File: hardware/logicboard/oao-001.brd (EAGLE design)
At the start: 100 x 80 mm, 9 parts, among them K1 G5V1, T1 2SC1815

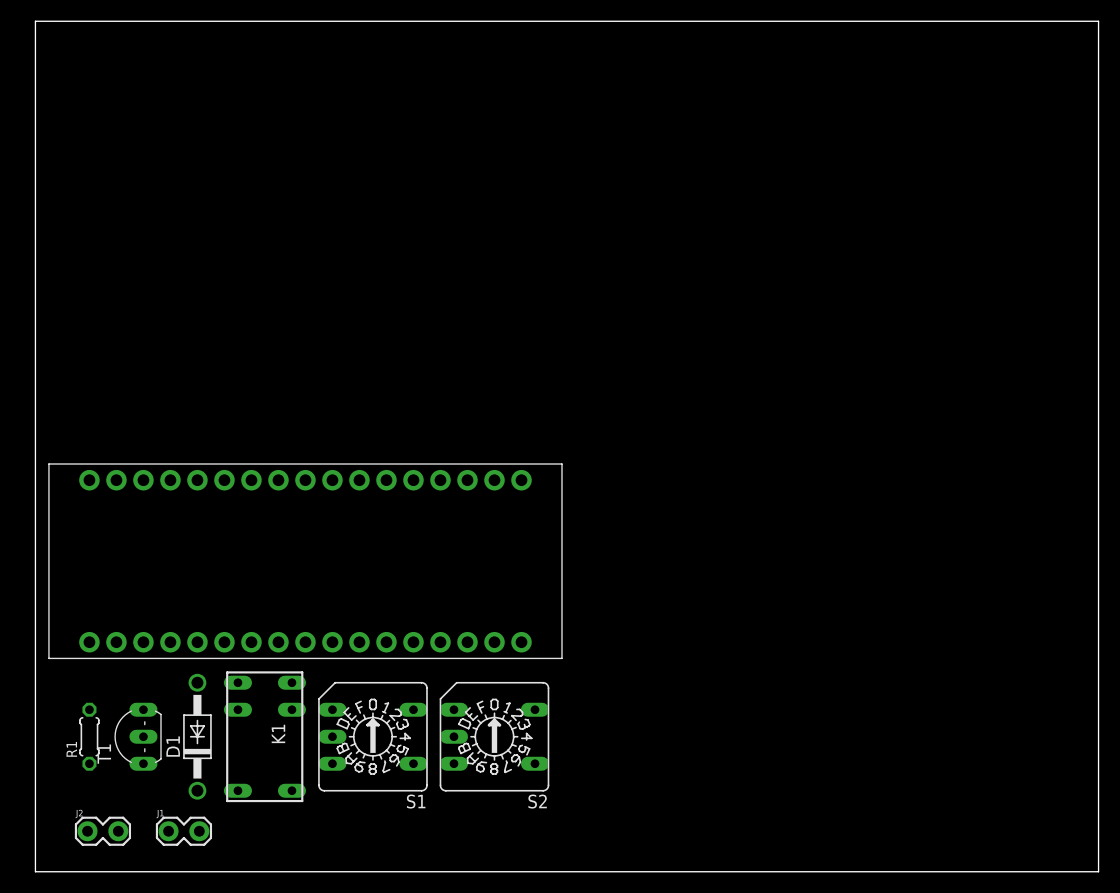
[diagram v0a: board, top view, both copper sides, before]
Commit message: Shrinked logicboard size.
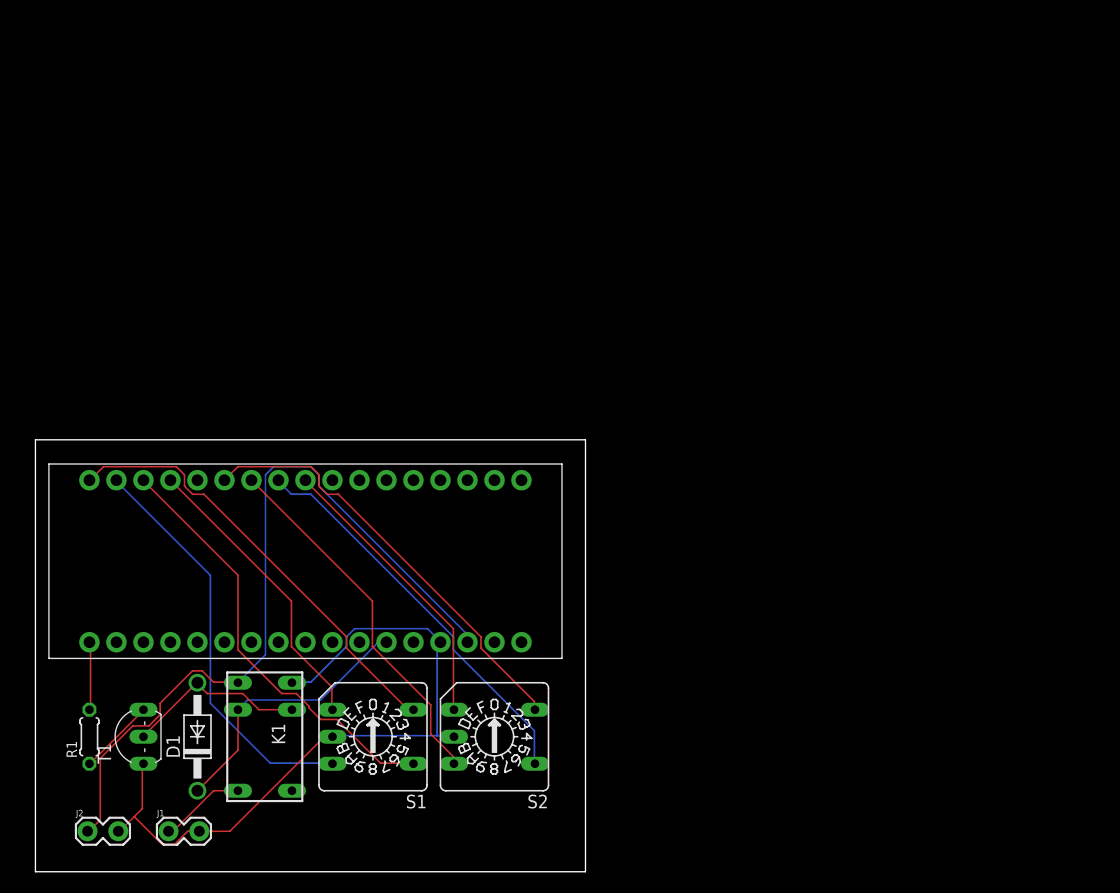
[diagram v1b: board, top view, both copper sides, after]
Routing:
- net VDD: track 0.00 -> 72.8 mm
- net GND: track 0.00 -> 68.9 mm
- net N$7: track 0.00 -> 41.7 mm
- net N$5: track 0.00 -> 40.9 mm
- net N$9: track 0.00 -> 40.7 mm
- net N$8: track 0.00 -> 38.5 mm
- net N$11: track 0.00 -> 37.7 mm
- net N$6: track 0.00 -> 34.6 mm
- net N$10: track 0.00 -> 27.9 mm
- net N$12: track 0.00 -> 27.4 mm
- net VCC: track 0.00 -> 25.8 mm
- net N$4: track 0.00 -> 17.3 mm
- net N$1: track 0.00 -> 8.11 mm
- net N$3: track 0.00 -> 7.28 mm
- net N$2: track 0.00 -> 6.49 mm
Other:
- board size 100 x 80 mm -> 51.7 x 40.6 mm

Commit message: Released hardware.
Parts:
- removed J1, J2: (no value), SparkFun-Connectors:1X02_LOCK
- added D2: (no value), SparkFun-LED:LED_3MM-NS
- added R2: 220, resistor:0204/5
- added S3: NC: 5V, NO: 12V, SparkFun-Switches:SWITCH_SPDT_PTH_11.6X4.0MM
- added VIN, VOUT: (no value), SparkFun-Connectors:1X02_LOCK
- R1: value (none) -> 3.3k
- moved S1 4.58 mm to (29.2, 16.5)
- moved S2 4.58 mm to (40.6, 16.5)
- moved D1 3.59 mm to (12.7, 15.2)
- moved K1 3.59 mm to (19.1, 15.2)
- moved U$1 3.59 mm to (22.9, 31.8)
- moved R1 2.84 mm to (3.81, 15.2)
- moved T1 2.84 mm to (8.89, 15.2)
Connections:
- new net N$13: R2.1, U$1.P$11
- new net N$14: D2.K, R2.2
- new net N$15: S3.3, U$1.P$20
- net GND: now also VIN.2, VOUT.2; no longer J1.2, J2.2
- net N$1: now also VOUT.1; no longer J1.1
- net VCC: now also D2.A, S3.1
- net VDD: now also S3.2, VIN.1; no longer J2.1, U$1.P$20
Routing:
- net N$13: track 0.00 -> 38.9 mm
- net VCC: track 25.8 -> 63.2 mm
- net VDD: track 72.8 -> 35.6 mm
- net N$15: track 0.00 -> 32.6 mm
- net GND: track 68.9 -> 61.6 mm
- net N$8: track 38.5 -> 35.0 mm
- net N$1: track 8.11 -> 4.94 mm
- net N$14: track 0.00 -> 2.58 mm
- net N$7: track 41.7 -> 39.5 mm
- net N$11: track 37.7 -> 39.0 mm
- net N$10: track 27.9 -> 26.7 mm
- net N$12: track 27.4 -> 26.2 mm
- net N$9: track 40.7 -> 39.7 mm
- net N$6: track 34.6 -> 33.7 mm
- net N$4: track 17.3 -> 16.6 mm
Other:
- board size 51.7 x 40.6 mm -> 47 x 47 mm
- board text added: "12V"
- board text added: "5V"
- board text added: "ON-AND-OFF Rev. 1 by Pineapple.cc"

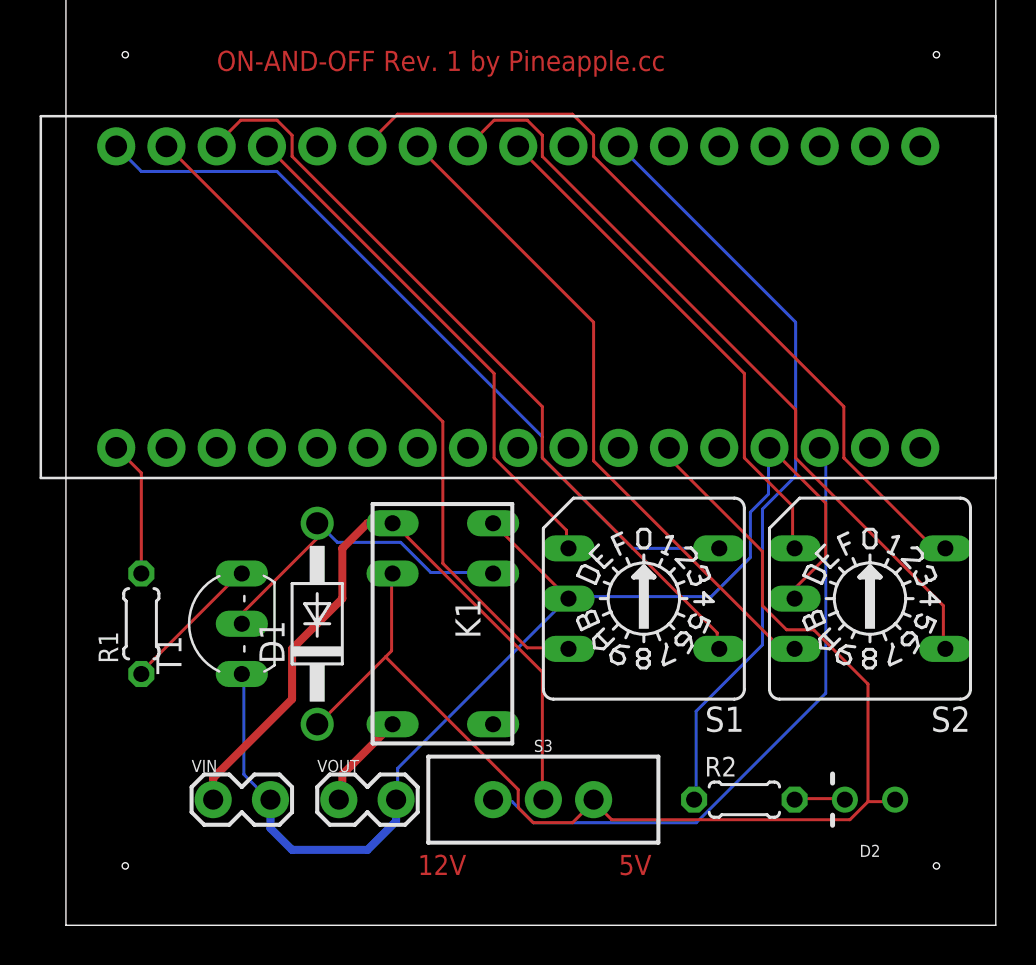
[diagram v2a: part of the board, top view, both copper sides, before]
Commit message: Added capacitor.
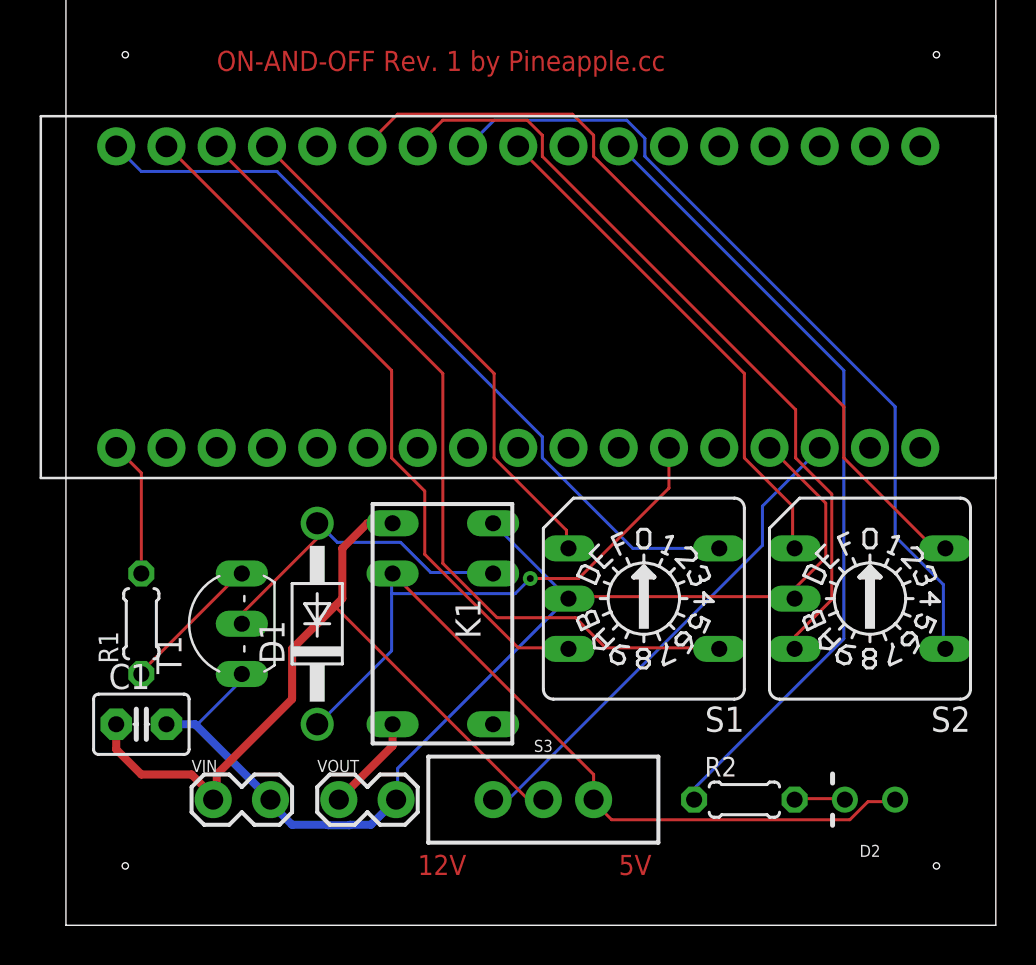
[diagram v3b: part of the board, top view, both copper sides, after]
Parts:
- added C1: (no value), capacitor-wima:C2.5-3
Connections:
- net GND: now also C1.2
- net VDD: now also C1.1
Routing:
- net N$15: track 32.6 -> 25.1 mm
- net N$6: track 33.7 -> 40.0 mm
- net VDD: track 35.6 -> 40.4 mm
- net VCC: track 63.2 -> 59.3 mm, vias 0 -> 1
- net GND: track 61.6 -> 58.1 mm
- net N$11: track 39.0 -> 42.0 mm
- net N$13: track 38.9 -> 40.9 mm
- net N$9: track 39.7 -> 41.6 mm

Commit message: Changed configuration (a little bit.)
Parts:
- moved T1 2.84 mm to (7.62, 17.8)
- moved R1 2.84 mm to (2.54, 17.8)
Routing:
- net N$2: track 6.88 -> 3.84 mm
- net GND: track 58.1 -> 60.1 mm
- net VDD: track 40.4 -> 41.2 mm
- net N$4: track 16.6 -> 16.1 mm
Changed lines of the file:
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@@
 <attribute name="OC_NEWARK" value="36M6377" x="19.05" y="15.24" size="1.778" layer="27" rot="R270" display="off"/>
 </element>
-<element name="R1" library="resistor" library_urn="urn:adsk.eagle:library:348" package="0204/5" package3d_urn="urn:adsk.eagle:package:25955/1" value="3.3k" x="3.81" y="15.24" rot="R90"/>
+<element name="R1" library="resistor" library_urn="urn:adsk.eagle:library:348" package="0204/5" package3d_urn="urn:adsk.eagle:package:25955/1" value="3.3k" x="2.54" y="17.78" rot="R90"/>
 <element name="S1" library="switch-dil" library_urn="urn:adsk.eagle:library:375" package="A1353HEX" package3d_urn="urn:adsk.eagle:package:27207/1" value="" x="29.21" y="16.51" rot="R180">
 <attribute name="MF" value="" x="29.21" y="16.51" size="1.778" layer="27" rot="R180" display="off"/>
@@
 <attribute name="OC_NEWARK" value="unknown" x="40.64" y="16.51" size="1.778" layer="27" rot="R180" display="off"/>
 </element>
-<element name="T1" library="transistor" library_urn="urn:adsk.eagle:library:402" package="TO92-ECB" package3d_urn="urn:adsk.eagle:package:29929/2" value="2SC1815" x="8.89" y="15.24" rot="R90"/>
+<element name="T1" library="transistor" library_urn="urn:adsk.eagle:library:402" package="TO92-ECB" package3d_urn="urn:adsk.eagle:package:29929/2" value="2SC1815" x="7.62" y="17.78" rot="R90"/>
 <element name="U$1" library="adafruit" package="ARDUINOMICRO" value="ARDUINOMICRO" x="22.86" y="31.75"/>
 <element name="R2" library="resistor" library_urn="urn:adsk.eagle:library:348" package="0204/5" package3d_urn="urn:adsk.eagle:package:25955/1" value="220" x="34.29" y="6.35"/>
@@
 <wire x1="7.4422" y1="6.5278" x2="7.4422" y2="6.35" width="0.4064" layer="1"/>
 <wire x1="23.3172" y1="6.4008" x2="24.0792" y2="6.4008" width="0.1524" layer="1"/>
+<wire x1="24.0792" y1="6.4008" x2="24.13" y2="6.35" width="0.1524" layer="1"/>
 <wire x1="13.589" y1="16.129" x2="23.3172" y2="6.4008" width="0.1524" layer="1"/>
-<wire x1="24.0792" y1="6.4008" x2="24.13" y2="6.35" width="0.1524" layer="1"/>
+<wire x1="23.3172" y1="6.4008" x2="24.13" y2="6.35" width="0.1524" layer="1"/>
 </signal>
 <signal name="GND">
@@
 <wire x1="36.8808" y1="16.6116" x2="36.83" y2="16.51" width="0.1524" layer="1"/>
 <wire x1="35.6616" y1="24.0792" x2="35.56" y2="24.13" width="0.1524" layer="1"/>
-<wire x1="8.8392" y1="12.3444" x2="8.8392" y2="12.6492" width="0.1524" layer="16"/>
-<wire x1="6.7056" y1="10.2108" x2="8.8392" y2="12.3444" width="0.1524" layer="16"/>
-<wire x1="8.8392" y1="12.6492" x2="8.89" y2="12.7" width="0.1524" layer="16"/>
+<wire x1="7.62" y1="11.1252" x2="7.62" y2="15.24" width="0.1524" layer="16"/>
+<wire x1="6.7056" y1="10.2108" x2="7.62" y2="11.1252" width="0.1524" layer="16"/>
 <wire x1="6.7056" y1="10.2108" x2="6.5278" y2="10.16" width="0.1524" layer="16"/>
-<wire x1="21.59" y1="20.32" x2="25.4" y2="16.51" width="0.1524" layer="16"/>
+<wire x1="25.4" y1="16.51" x2="21.59" y2="20.32" width="0.1524" layer="16"/>
 <wire x1="16.764" y1="7.9248" x2="16.764" y2="6.4008" width="0.1524" layer="16"/>
 <wire x1="25.2984" y1="16.4592" x2="16.764" y2="7.9248" width="0.1524" layer="16"/>
@@
 <contactref element="U$1" pad="P$34"/>
 <contactref element="R1" pad="2"/>
-<wire x1="3.81" y1="22.86" x2="3.81" y2="17.78" width="0.1524" layer="1"/>
-<wire x1="2.54" y1="24.13" x2="3.81" y2="22.86" width="0.1524" layer="1"/>
+<wire x1="2.5908" y1="24.0792" x2="2.5908" y2="20.4216" width="0.1524" layer="1"/>
+<wire x1="2.5908" y1="20.4216" x2="2.54" y2="20.32" width="0.1524" layer="1"/>
+<wire x1="2.5908" y1="24.0792" x2="2.54" y2="24.13" width="0.1524" layer="1"/>
 </signal>
 <signal name="N$3">
 <contactref element="R1" pad="1"/>
 <contactref element="T1" pad="B"/>
-<wire x1="8.8392" y1="17.8308" x2="3.81" y2="12.8016" width="0.1524" layer="1"/>
-<wire x1="3.81" y1="12.8016" x2="3.81" y2="12.7" width="0.1524" layer="1"/>
-<wire x1="8.8392" y1="17.8308" x2="8.89" y2="17.78" width="0.1524" layer="1"/>
+<wire x1="7.62" y1="20.2692" x2="2.5908" y2="15.24" width="0.1524" layer="1"/>
+<wire x1="2.5908" y1="15.24" x2="2.54" y2="15.24" width="0.1524" layer="1"/>
+<wire x1="7.62" y1="20.2692" x2="7.62" y2="20.32" width="0.1524" layer="1"/>
 </signal>
 <signal name="N$4">
@@
 <contactref element="K1" pad="9"/>
 <contactref element="D1" pad="A"/>
-<wire x1="8.9916" y1="15.8496" x2="8.9916" y2="15.24" width="0.1524" layer="1"/>
-<wire x1="12.6492" y1="19.5072" x2="8.9916" y2="15.8496" width="0.1524" layer="1"/>
-<wire x1="12.6492" y1="20.2692" x2="12.6492" y2="19.5072" width="0.1524" layer="1"/>
-<wire x1="8.9916" y1="15.24" x2="8.89" y2="15.24" width="0.1524" layer="1"/>
-<wire x1="12.6492" y1="20.2692" x2="12.7" y2="20.32" width="0.1524" layer="1"/>
+<wire x1="10.2108" y1="17.8308" x2="7.62" y2="17.8308" width="0.1524" layer="1"/>
+<wire x1="12.7" y1="20.32" x2="10.2108" y2="17.8308" width="0.1524" layer="1"/>
+<wire x1="7.62" y1="17.8308" x2="7.62" y2="17.78" width="0.1524" layer="1"/>
 <wire x1="18.4404" y1="17.8308" x2="21.4884" y2="17.8308" width="0.1524" layer="16"/>
 <wire x1="16.9164" y1="19.3548" x2="18.4404" y2="17.8308" width="0.1524" layer="16"/>
@@
 <contactref element="R2" pad="1"/>
 <wire x1="31.8516" y1="7.0104" x2="31.8516" y2="6.4008" width="0.1524" layer="16"/>
+<wire x1="31.8516" y1="6.4008" x2="31.75" y2="6.35" width="0.1524" layer="16"/>
 <wire x1="39.3192" y1="14.478" x2="31.8516" y2="7.0104" width="0.1524" layer="16"/>
 <wire x1="39.3192" y1="28.0416" x2="39.3192" y2="14.478" width="0.1524" layer="16"/>
 <wire x1="28.0416" y1="39.3192" x2="39.3192" y2="28.0416" width="0.1524" layer="16"/>
-<wire x1="31.8516" y1="6.4008" x2="31.75" y2="6.35" width="0.1524" layer="16"/>
 <wire x1="28.0416" y1="39.3192" x2="27.94" y2="39.37" width="0.1524" layer="16"/>
 </signal>
